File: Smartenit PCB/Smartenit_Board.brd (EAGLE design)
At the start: 55.3 x 72.5 mm, 85 parts, among them J3 2X5CONNECTOR1.27MM, Q1 QUARTZ_3.58M_2PIN, U1 ADE7953, U2 ESP-WROOM-32, U3 SN74LVC1G3157

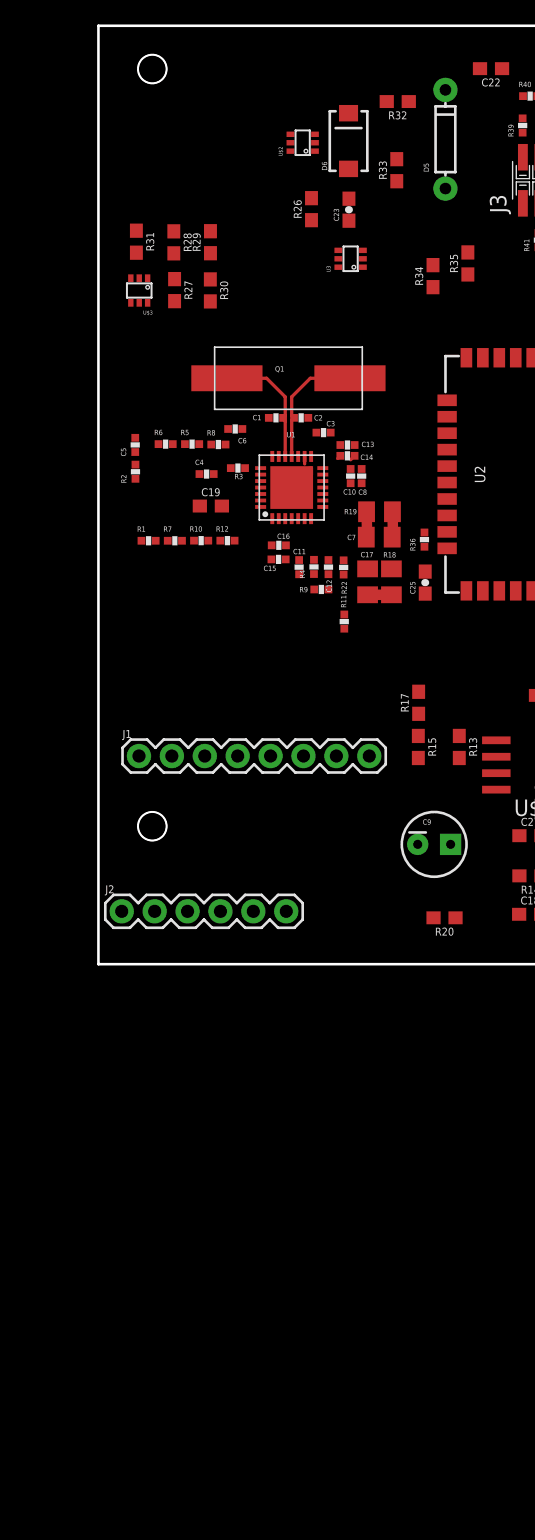
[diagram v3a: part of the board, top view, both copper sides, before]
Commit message: changed 2mm headers
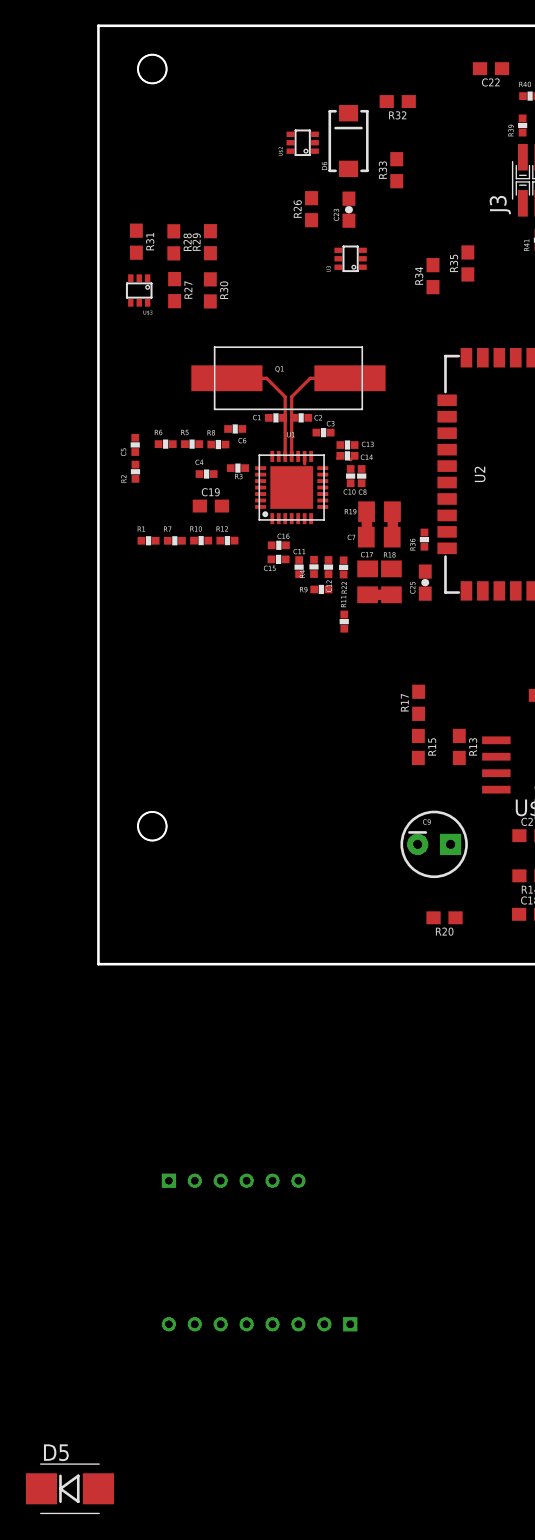
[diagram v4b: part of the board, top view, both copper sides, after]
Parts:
- removed J1: (no value), SparkFun-Connectors:1X08
- removed J2: (no value), SparkFun-Connectors:1X06
- added U$4: 2MM_CONN8, Smart_Charger:CONN82MM
- added U$5: CONN6_2MM, Smart_Charger:CONN6_2MM
- D5: device SparkFun:DIODE-1N4148 -> SparkFun:SMB-DIODE
- moved D5 108.1 mm to (-2.20, -113.0), turned to 0 degrees
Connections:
- net -12V: now also U$5.4; no longer J2.3
- net 12V: now also U$5.6; no longer J2.1
- net DIO11: now also U$5.2; no longer J2.5
- net DIO12: now also U$5.3; no longer J2.4
- net GND: now also U$4.7, U$5.5; no longer J1.2, J2.2
- net IAN: now also U$4.2; no longer J1.7
- net IAP: now also U$4.1; no longer J1.8
- net IBN: now also U$4.4; no longer J1.5
- net IBP: now also U$4.3; no longer J1.6
- net LNV1: now also U$4.5; no longer J1.4
- net LNV2: now also U$4.6; no longer J1.3
- net N$38: now also U$5.1; no longer J2.6
- net PILOT: now also U$4.8; no longer J1.1
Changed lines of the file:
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@@
 <element name="C4" library="Nizanlib" package="0402-CAP" value="104n" x="8.35" y="-34.61"/>
 <element name="C9" library="SparkFun" package="CPOL-RADIAL-10UF-25V" value="" x="25.92" y="-63.2"/>
-<element name="J1" library="SparkFun-Connectors" package="1X08" value="" x="3.13" y="-56.38">
-<attribute name="PROD_ID" value="CONN-08438" x="3.13" y="-56.38" size="1.778" layer="27" display="off"/>
-</element>
-<element name="J2" library="SparkFun-Connectors" package="1X06" value="" x="1.8" y="-68.37">
-<attribute name="PROD_ID" value="CONN-08437" x="1.8" y="-68.37" size="1.778" layer="27" display="off"/>
-</element>
 <element name="U$1" library="Smart_Charger" package="SOIC8" value="MP1584" x="33.32" y="-57.07" rot="R90"/>
 <element name="R13" library="SparkFun-Resistors" package="0603" value="100k" x="27.86" y="-55.68" rot="R270">
@@
 <attribute name="PROD_ID" value="CAP-09232" x="30.31" y="-3.31" size="1.778" layer="27" rot="R180" display="off"/>
 </element>
-<element name="D5" library="SparkFun" package="DIODE-1N4148" value="" x="26.79" y="-8.76" rot="R90"/>
+<element name="D5" library="SparkFun" package="SMB-DIODE" value="" x="-2.2" y="-112.95"/>
 <element name="D6" library="SparkFun" package="SMA-DIODE" value="" x="19.31" y="-8.9" rot="R90"/>
 <element name="C23" library="SparkFun" package="0603-CAP" value="10uF/6.3V" x="19.34" y="-14.2" rot="R90"/>
@@
 <element name="C25" library="SparkFun" package="0603-CAP" value="104" x="25.23" y="-42.99" rot="R90"/>
 <element name="R36" library="Nizanlib" package="0402-RES" value="12k" x="25.17" y="-39.67" rot="R90"/>
+<element name="U$5" library="Smart_Charger" package="CONN6_2MM" value="CONN6_2MM" x="5.44" y="-89.17"/>
+<element name="U$4" library="Smart_Charger" package="CONN82MM" value="2MM_CONN8" x="5.44" y="-100.25"/>
 </elements>
 <signals>
@@
 <contactref element="R5" pad="2"/>
 <contactref element="R12" pad="1"/>
-<contactref element="J1" pad="6"/>
-<wire x1="9.41" y1="-39.75" x2="15.83" y2="-56.38" width="0" layer="19" extent="1-1"/>
+<contactref element="U$4" pad="3"/>
+<wire x1="9.41" y1="-39.75" x2="15.44" y2="-100.25" width="0" layer="19" extent="1-1"/>
 <wire x1="7.78" y1="-32.3" x2="9.41" y2="-39.75" width="0" layer="19" extent="1-1"/>
 </signal>
@@
 <contactref element="R6" pad="1"/>
 <contactref element="R7" pad="1"/>
-<contactref element="J1" pad="5"/>
-<wire x1="5.35" y1="-39.76" x2="13.29" y2="-56.38" width="0" layer="19" extent="1-1"/>
+<contactref element="U$4" pad="4"/>
+<wire x1="5.35" y1="-39.76" x2="13.44" y2="-100.25" width="0" layer="19" extent="1-1"/>
 <wire x1="4.64" y1="-32.3" x2="5.35" y2="-39.76" width="0" layer="19" extent="1-1"/>
 </signal>
@@
 <contactref element="R17" pad="1"/>
 <contactref element="C19" pad="1"/>
-<contactref element="J2" pad="2"/>
-<contactref element="J1" pad="2"/>
 <contactref element="S1" pad="1"/>
 <contactref element="J3" pad="10"/>
@@
 <contactref element="C25" pad="2"/>
 <contactref element="R36" pad="1"/>
-<wire x1="5.67" y1="-56.38" x2="4.34" y2="-68.37" width="0" layer="19" extent="1-1"/>
-<wire x1="18.98" y1="-46.55" x2="5.67" y2="-56.38" width="0" layer="19" extent="1-1"/>
+<contactref element="U$5" pad="5"/>
+<contactref element="U$4" pad="7"/>
+<wire x1="13.44" y1="-89.17" x2="7.44" y2="-100.25" width="0" layer="19" extent="1-1"/>
+<wire x1="24.65" y1="-63.2" x2="13.44" y2="-89.17" width="0" layer="19" extent="1-1"/>
+<wire x1="24.7" y1="-54.83" x2="24.65" y2="-63.2" width="0" layer="19" extent="1-1"/>
+<wire x1="24.72" y1="-53.12" x2="24.7" y2="-54.83" width="0" layer="19" extent="1-1"/>
+<wire x1="27.86" y1="-54.83" x2="24.7" y2="-54.83" width="0" layer="19" extent="1-1"/>
+<wire x1="30.72" y1="-55.165" x2="27.86" y2="-54.83" width="0" layer="19" extent="1-1"/>
+<wire x1="18.98" y1="-46.55" x2="24.72" y2="-53.12" width="0" layer="19" extent="1-1"/>
 <wire x1="17.76" y1="-43.52" x2="18.98" y2="-46.55" width="0" layer="19" extent="1-1"/>
 <wire x1="17.761" y1="-42.344" x2="17.76" y2="-43.52" width="0" layer="19" extent="1-1"/>
@@
 <wire x1="3.32" y1="-39.76" x2="8.48" y2="-39.75" width="0" layer="19" extent="1-1"/>
 <wire x1="26.92" y1="-28.915" x2="19.778" y2="-32.368" width="0" layer="19" extent="1-1"/>
-<wire x1="24.72" y1="-53.12" x2="18.98" y2="-46.55" width="0" layer="19" extent="1-1"/>
-<wire x1="24.7" y1="-54.83" x2="24.72" y2="-53.12" width="0" layer="19" extent="1-1"/>
-<wire x1="27.86" y1="-54.83" x2="24.7" y2="-54.83" width="0" layer="19" extent="1-1"/>
-<wire x1="30.72" y1="-55.165" x2="27.86" y2="-54.83" width="0" layer="19" extent="1-1"/>
-<wire x1="24.65" y1="-63.2" x2="24.7" y2="-54.83" width="0" layer="19" extent="1-1"/>
 <wire x1="40.2" y1="-54.73" x2="30.72" y2="-55.165" width="0" layer="19" extent="1-1"/>
 <wire x1="41.95" y1="-54.74" x2="40.2" y2="-54.73" width="0" layer="19" extent="1-1"/>
@@
 <wire x1="16.72" y1="-9.68" x2="19.31" y2="-11.05" width="0" layer="19" extent="1-1"/>
 <wire x1="23.03" y1="-12" x2="19.31" y2="-11.05" width="0" layer="19" extent="1-1"/>
-<wire x1="26.79" y1="-12.57" x2="23.03" y2="-12" width="0" layer="19" extent="1-1"/>
-<wire x1="31.16" y1="-3.31" x2="26.79" y2="-12.57" width="0" layer="19" extent="1-1"/>
-<wire x1="37.85" y1="-10.15" x2="31.16" y2="-3.31" width="0" layer="19" extent="1-1"/>
-<wire x1="37.74" y1="-6.53" x2="37.85" y2="-10.15" width="0" layer="19" extent="1-1"/>
+<wire x1="0" y1="-112.95" x2="23.03" y2="-12" width="0" layer="19" extent="1-1"/>
+<wire x1="31.16" y1="-3.31" x2="0" y2="-112.95" width="0" layer="19" extent="1-1"/>
+<wire x1="37.74" y1="-6.53" x2="31.16" y2="-3.31" width="0" layer="19" extent="1-1"/>
+<wire x1="37.85" y1="-10.15" x2="37.74" y2="-6.53" width="0" layer="19" extent="1-1"/>
 </signal>
 <signal name="DIO0">
@@
 <contactref element="R9" pad="2"/>
 <contactref element="R4" pad="1"/>
-<contactref element="J1" pad="8"/>
-<wire x1="16.66" y1="-43.52" x2="20.91" y2="-56.38" width="0" layer="19" extent="1-1"/>
+<contactref element="U$4" pad="1"/>
+<wire x1="16.66" y1="-43.52" x2="19.44" y2="-100.25" width="0" layer="19" extent="1-1"/>
 <wire x1="16.64" y1="-42.33" x2="16.66" y2="-43.52" width="0" layer="19" extent="1-1"/>
 </signal>
@@
 <contactref element="R11" pad="1"/>
 <contactref element="R22" pad="1"/>
-<contactref element="J1" pad="7"/>
-<wire x1="18.98" y1="-45.45" x2="18.37" y2="-56.38" width="0" layer="19" extent="1-1"/>
+<contactref element="U$4" pad="2"/>
+<wire x1="18.98" y1="-45.45" x2="17.44" y2="-100.25" width="0" layer="19" extent="1-1"/>
 <wire x1="18.93" y1="-42.37" x2="18.98" y2="-45.45" width="0" layer="19" extent="1-1"/>
 </signal>
@@
 <contactref element="R14" pad="2"/>
 <contactref element="C20" pad="2"/>
-<contactref element="J2" pad="1"/>
 <contactref element="U$3" pad="4"/>
 <contactref element="R27" pad="1"/>
-<wire x1="32.5" y1="-65.63" x2="1.8" y2="-68.37" width="0" layer="19" extent="1-1"/>
+<contactref element="U$5" pad="6"/>
+<wire x1="32.5" y1="-65.63" x2="15.44" y2="-89.17" width="0" layer="19" extent="1-1"/>
 <wire x1="30.72" y1="-57.705" x2="32.5" y2="-65.63" width="0" layer="19" extent="1-1"/>
 <wire x1="38.5" y1="-54.73" x2="30.72" y2="-57.705" width="0" layer="19" extent="1-1"/>
@@
 </signal>
 <signal name="PILOT">
-<contactref element="J1" pad="1"/>
 <contactref element="R31" pad="2"/>
 <contactref element="R32" pad="2"/>
 <contactref element="D6" pad="C"/>
-<wire x1="2.93" y1="-17.52" x2="3.13" y2="-56.38" width="0" layer="19" extent="1-1"/>
+<contactref element="U$4" pad="8"/>
+<wire x1="2.93" y1="-17.52" x2="5.44" y2="-100.25" width="0" layer="19" extent="1-1"/>
 <wire x1="19.31" y1="-6.75" x2="2.93" y2="-17.52" width="0" layer="19" extent="1-1"/>
 <wire x1="22.26" y1="-5.85" x2="19.31" y2="-6.75" width="0" layer="19" extent="1-1"/>
 </signal>
 <signal name="LNV2">
-<contactref element="J1" pad="3"/>
 <contactref element="R34" pad="1"/>
-<wire x1="25.83" y1="-20.18" x2="8.21" y2="-56.38" width="0" layer="19" extent="1-1"/>
+<contactref element="U$4" pad="6"/>
+<wire x1="25.83" y1="-20.18" x2="9.44" y2="-100.25" width="0" layer="19" extent="1-1"/>
 </signal>
 <signal name="LNV1">
-<contactref element="J1" pad="4"/>
 <contactref element="R35" pad="1"/>
-<wire x1="28.52" y1="-19.2" x2="10.75" y2="-56.38" width="0" layer="19" extent="1-1"/>
-</signal>
-<signal name="DIO12">
-<contactref element="J2" pad="4"/>
-</signal>
-<signal name="DIO11">
-<contactref element="J2" pad="5"/>
+<contactref element="U$4" pad="5"/>
+<wire x1="28.52" y1="-19.2" x2="11.44" y2="-100.25" width="0" layer="19" extent="1-1"/>
 </signal>
 <signal name="N$38">
-<contactref element="J2" pad="6"/>
 <contactref element="R20" pad="2"/>
-<wire x1="25.87" y1="-68.87" x2="14.5" y2="-68.37" width="0" layer="19" extent="1-1"/>
+<contactref element="U$5" pad="1"/>
+<wire x1="25.87" y1="-68.87" x2="5.44" y2="-89.17" width="0" layer="19" extent="1-1"/>
 </signal>
 <signal name="-12V">
-<contactref element="J2" pad="3"/>
 <contactref element="U$3" pad="1"/>
 <contactref element="R29" pad="1"/>
 <contactref element="C22" pad="2"/>
-<wire x1="3.8" y1="-19.49" x2="6.88" y2="-68.37" width="0" layer="19" extent="1-1"/>
+<contactref element="U$5" pad="4"/>
+<wire x1="3.8" y1="-19.49" x2="11.44" y2="-89.17" width="0" layer="19" extent="1-1"/>
 <wire x1="8.65" y1="-17.56" x2="3.8" y2="-19.49" width="0" layer="19" extent="1-1"/>
 <wire x1="29.46" y1="-3.31" x2="8.65" y2="-17.56" width="0" layer="19" extent="1-1"/>
@@
 <contactref element="R33" pad="2"/>
 <contactref element="D5" pad="C"/>
-<wire x1="23.96" y1="-5.85" x2="26.79" y2="-4.95" width="0" layer="19" extent="1-1"/>
+<wire x1="23.96" y1="-5.85" x2="-4.4" y2="-112.95" width="0" layer="19" extent="1-1"/>
 <wire x1="23.03" y1="-10.3" x2="23.96" y2="-5.85" width="0" layer="19" extent="1-1"/>
 </signal>
@@
 <wire x1="26.92" y1="-40.345" x2="38.51" y2="-19.15" width="0" layer="19" extent="1-1"/>
 </signal>
+<signal name="DIO12">
+<contactref element="U$5" pad="3"/>
+</signal>
+<signal name="DIO11">
+<contactref element="U$5" pad="2"/>
+</signal>
 </signals>

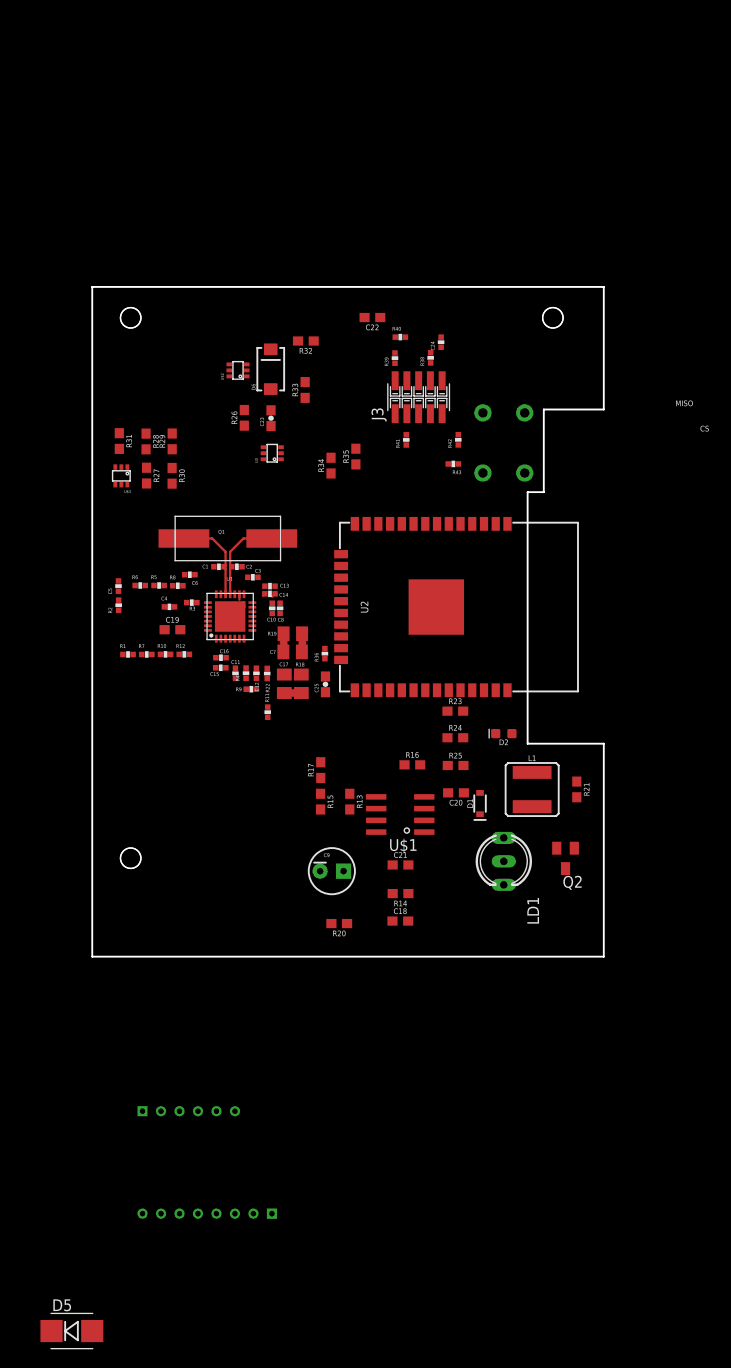
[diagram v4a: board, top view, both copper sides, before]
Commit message: new positions and dimensions
updated new part positions and new dimensions for holes and headers
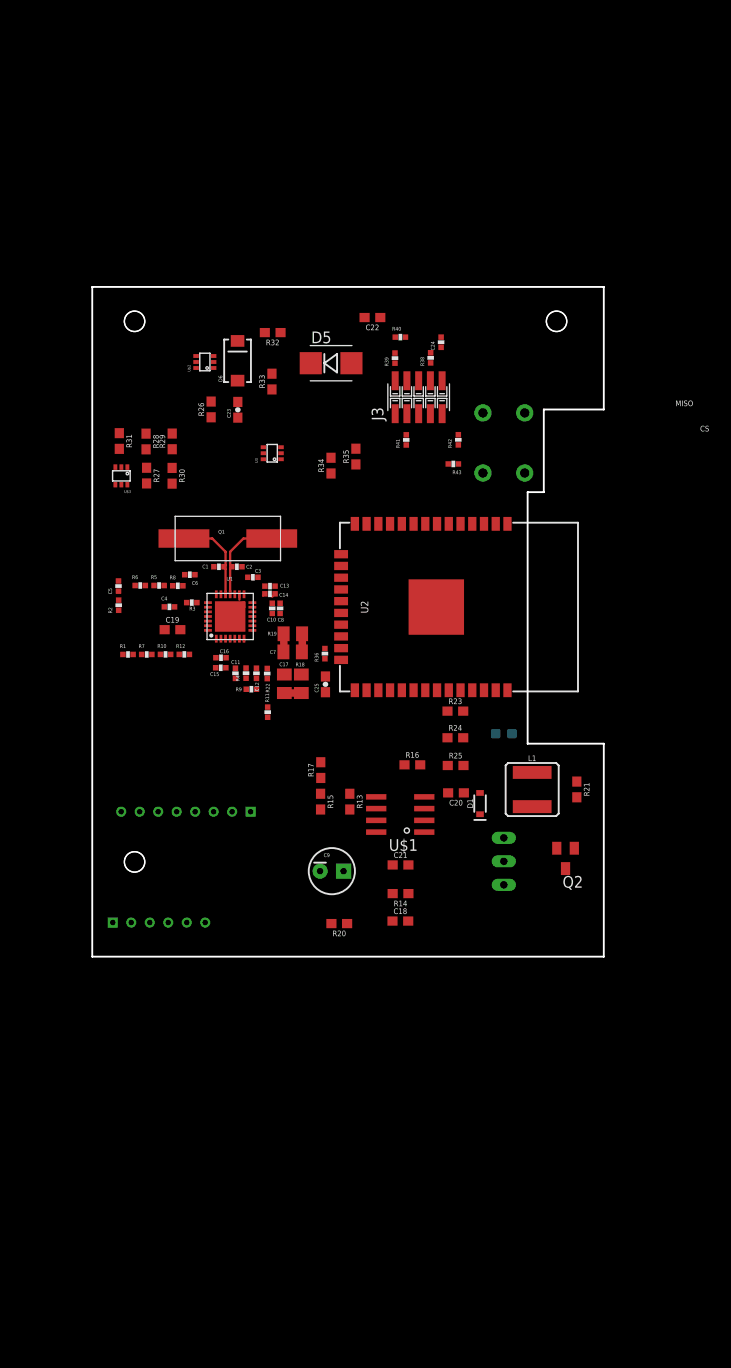
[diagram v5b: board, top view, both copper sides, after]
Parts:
- moved D5 108.4 mm to (25.8, -8.25)
- moved U$4 43.5 mm to (3.13, -56.8)
- moved U$5 20.7 mm to (2.22, -68.8)
- moved C23 3.70 mm to (15.8, -13.3)
- moved R26 3.70 mm to (12.9, -13.2)
- moved R32 3.70 mm to (19.5, -4.94)
- moved R33 3.70 mm to (19.4, -10.2)
- moved D6 3.70 mm to (15.7, -7.99)
- moved U$2 3.70 mm to (13.1, -8.77)
- flipped D2 to the bottom
- flipped LD1 to the bottom
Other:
- outline, holes or cut-outs redrawn

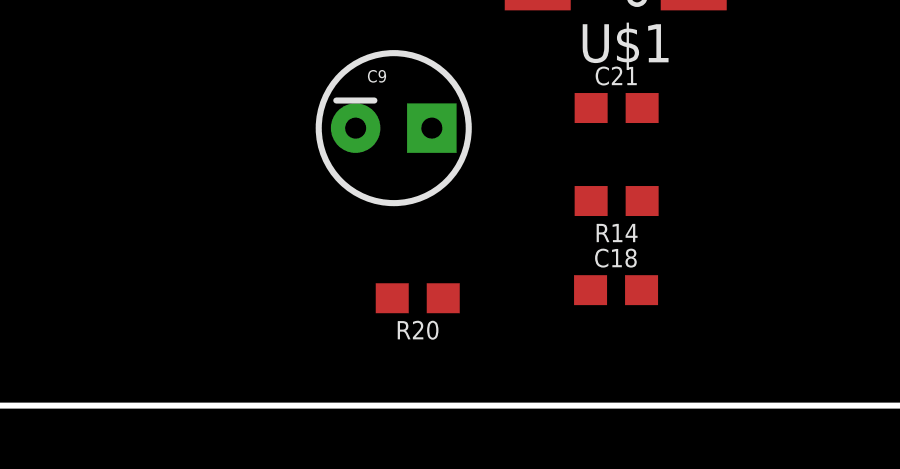
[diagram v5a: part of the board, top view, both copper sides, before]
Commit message: new update
moved resistor
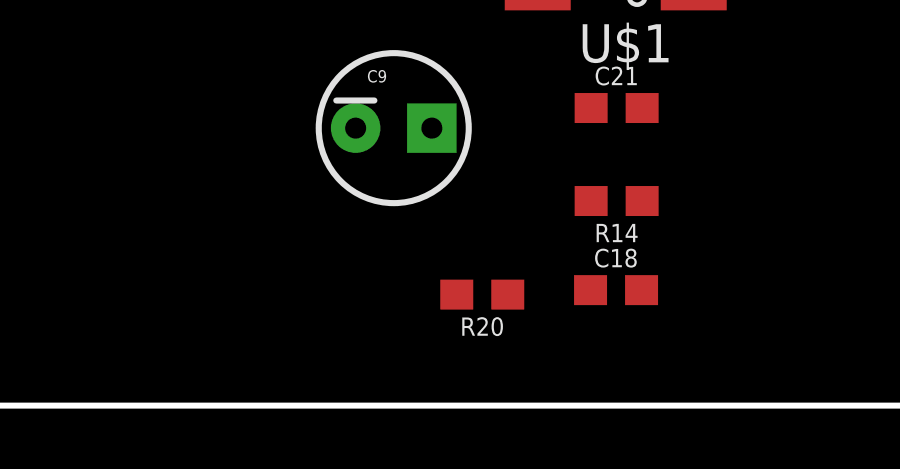
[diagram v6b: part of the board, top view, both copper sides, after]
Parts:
- moved R20 2.15 mm to (28.9, -68.8)
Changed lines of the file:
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@@
 <attribute name="PROD_ID" value="DIO-09646" x="41.95" y="-55.89" size="1.778" layer="27" rot="R90" display="off"/>
 </element>
-<element name="R20" library="SparkFun-Resistors" package="0603" value="100k" x="26.72" y="-68.87" rot="R180">
-<attribute name="PROD_ID" value="RES-07828" x="26.72" y="-68.87" size="1.778" layer="27" rot="R180" display="off"/>
+<element name="R20" library="SparkFun-Resistors" package="0603" value="100k" x="28.87" y="-68.75" rot="R180">
+<attribute name="PROD_ID" value="RES-07828" x="28.87" y="-68.75" size="1.778" layer="27" rot="R180" display="off"/>
 </element>
 <element name="Q2" library="semicon-smd-ipc" library_urn="urn:adsk.eagle:library:353" package="SOT23" package3d_urn="urn:adsk.eagle:package:26310/1" value="" x="51.2" y="-61.82" rot="R180"/>
@@
 <contactref element="R20" pad="2"/>
 <contactref element="U$5" pad="1"/>
-<wire x1="25.87" y1="-68.87" x2="2.22" y2="-68.76" width="0" layer="19" extent="1-1"/>
+<wire x1="28.02" y1="-68.75" x2="2.22" y2="-68.76" width="0" layer="19" extent="1-1"/>
 </signal>
 <signal name="-12V">
@@
 <contactref element="R20" pad="1"/>
 <contactref element="Q2" pad="3"/>
-<wire x1="51.2" y1="-62.92" x2="27.57" y2="-68.87" width="0" layer="19" extent="1-1"/>
+<wire x1="51.2" y1="-62.92" x2="29.72" y2="-68.75" width="0" layer="19" extent="1-1"/>
 </signal>
 <signal name="DIO10">
